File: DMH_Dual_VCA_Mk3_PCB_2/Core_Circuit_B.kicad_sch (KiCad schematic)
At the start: 24 parts, among them Q3 BC548, Q4 BC548, U2 TL074

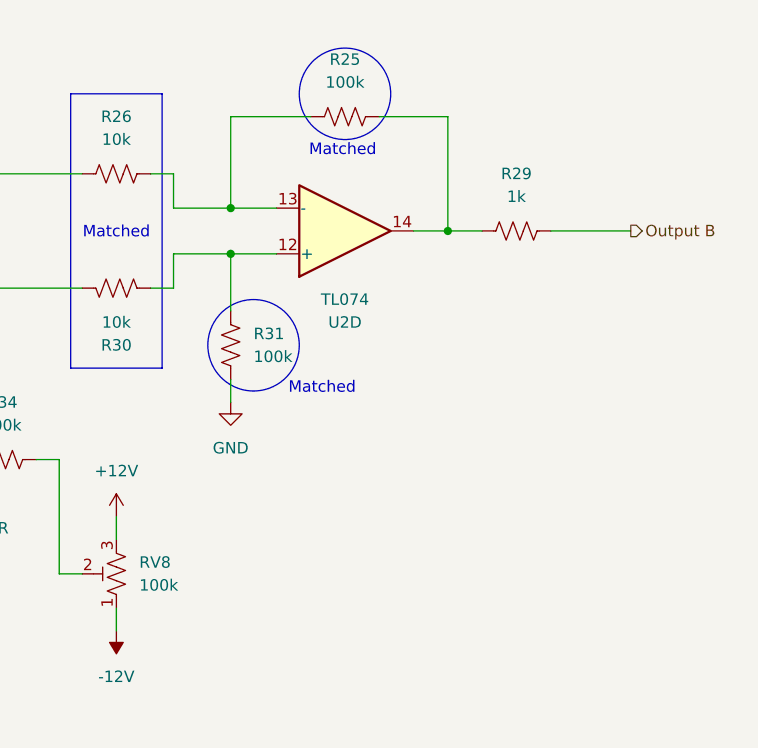
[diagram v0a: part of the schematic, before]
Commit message: Synced PCB 1 and 2 schematics
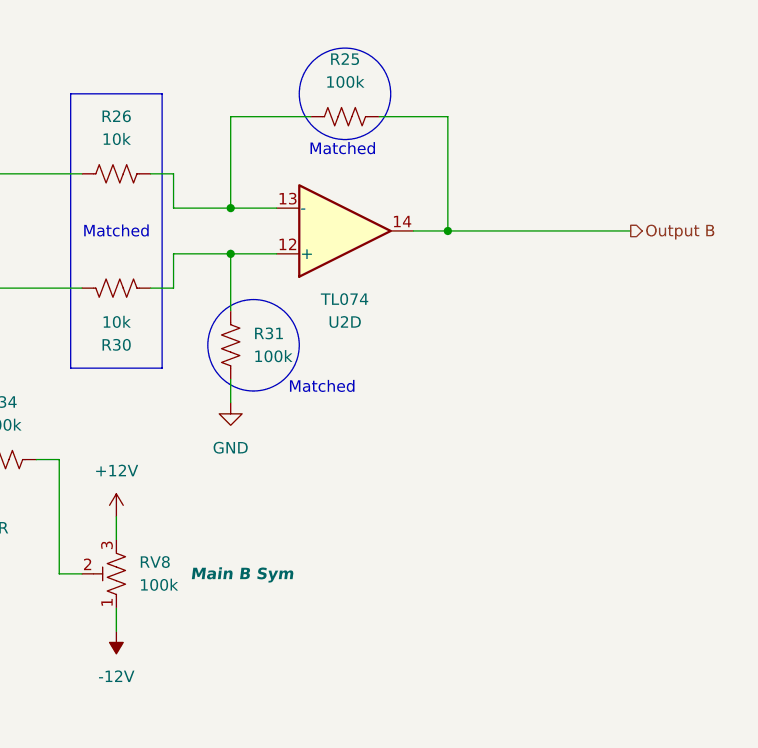
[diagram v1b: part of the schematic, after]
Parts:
- removed R29: 1k, Resistor_THT:R_Axial_DIN0207_L6.3mm_D2.5mm_P7.62mm_Horizontal, symbol Device:R_US
- RV8: Function (none) -> Main B Sym
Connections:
- net Output B: now also R25.1, U2.14
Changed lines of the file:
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@@
-	(wire
-		(pts
-			(xy 257.81 50.8) (xy 266.7 50.8)
-		)
-		(stroke
-			(width 0)
-			(type default)
-		)
-	)
 	(wire
 		(pts
@@
 	(wire
 		(pts
-			(xy 246.38 50.8) (xy 250.19 50.8)
+			(xy 246.38 50.8) (xy 266.7 50.8)
 		)
 		(stroke
@@
 	(symbol
 		(lib_id "Device:R_US")
-		(at 254 50.8 270)
-		(unit 1)
-		(exclude_from_sim no)
-		(in_bom yes)
-		(on_board yes)
-		(dnp no)
-		(fields_autoplaced yes)
-		(property "Reference" "R29"
-			(at 254 44.45 90)
-			(effects
-				(font
-					(size 1.27 1.27)
-				)
-			)
-		)
-		(property "Value" "1k"
-			(at 254 46.99 90)
-			(effects
-				(font
-					(size 1.27 1.27)
-				)
-			)
-		)
-		(property "Footprint" "Resistor_THT:R_Axial_DIN0207_L6.3mm_D2.5mm_P7.62mm_Horizontal"
-			(at 253.746 51.816 90)
-			(effects
-				(font
-					(size 1.27 1.27)
-				)
-				(hide yes)
-			)
-		)
-		(property "Datasheet" "~"
-			(at 254 50.8 0)
-			(effects
-				(font
-					(size 1.27 1.27)
-				)
-				(hide yes)
-			)
-		)
-		(property "Description" "Resistor, US symbol"
-			(at 254 50.8 0)
-			(effects
-				(font
-					(size 1.27 1.27)
-				)
-				(hide yes)
-			)
-		)
-		(property "Function" ""
-			(at 254 50.8 0)
-			(effects
-				(font
-					(size 1.27 1.27)
-				)
-			)
-		)
-		(pin "1"
-		)
-		(pin "2"
-		)
-		(instances
-			(project "DMH_Transistor_VCA_PCB"
-				(path "/58f4306d-5387-4983-bb08-41a2313fd315/7915b580-c9b0-4472-ab9c-d9fb99b1a92f"
-					(reference "R29")
-					(unit 1)
-				)
-			)
-		)
-	)
-	(symbol
-		(lib_id "Device:R_US")
 		(at 234.95 38.1 270)
 		(unit 1)
@@
 			)
 		)
+		(property "Sim.Device" "NPN"
+			(at 180.34 76.2 0)
+			(effects
+				(font
+					(size 1.27 1.27)
+				)
+				(hide yes)
+			)
+		)
+		(property "Sim.Pins" "1=C 2=B 3=E"
+			(at 180.34 76.2 0)
+			(effects
+				(font
+					(size 1.27 1.27)
+				)
+				(hide yes)
+			)
+		)
 		(pin "3"
 		)
@@
 		(exclude_from_sim no)
 		(in_bom yes)
-		(on_board yes)
+		(on_board no)
 		(dnp no)
 		(property "Reference" "U2"
@@
 		(exclude_from_sim no)
 		(in_bom yes)
-		(on_board yes)
+		(on_board no)
 		(dnp no)
 		(property "Reference" "U2"
@@
 		(exclude_from_sim no)
 		(in_bom yes)
-		(on_board yes)
+		(on_board no)
 		(dnp no)
 		(property "Reference" "U2"
@@
 		(on_board yes)
 		(dnp no)
-		(fields_autoplaced yes)
 		(property "Reference" "RV8"
 			(at 212.09 87.6299 0)
@@
 				)
 				(hide yes)
+			)
+		)
+		(property "Function" "Main B Sym"
+			(at 223.52 88.9 0)
+			(effects
+				(font
+					(size 1.27 1.27)
+					(thickness 0.254)
+					(bold yes)
+					(italic yes)
+				)
 			)
 		)
@@
 		)
 		(property "Description" "0.1A Ic, 30V Vce, Small Signal NPN Transistor, TO-92"
+			(at 149.86 76.2 0)
+			(effects
+				(font
+					(size 1.27 1.27)
+				)
+				(hide yes)
+			)
+		)
+		(property "Sim.Device" "NPN"
+			(at 149.86 76.2 0)
+			(effects
+				(font
+					(size 1.27 1.27)
+				)
+				(hide yes)
+			)
+		)
+		(property "Sim.Pins" "1=C 2=B 3=E"
 			(at 149.86 76.2 0)
 			(effects
@@
 		(exclude_from_sim no)
 		(in_bom yes)
-		(on_board yes)
+		(on_board no)
 		(dnp no)
 		(property "Reference" "U2"
